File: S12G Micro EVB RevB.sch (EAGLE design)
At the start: 42 parts, among them IC1 FT232RL, IC2 MCP1640, J1 JUMPER_2WAY, J2 JUMPER, J3 JUMPER

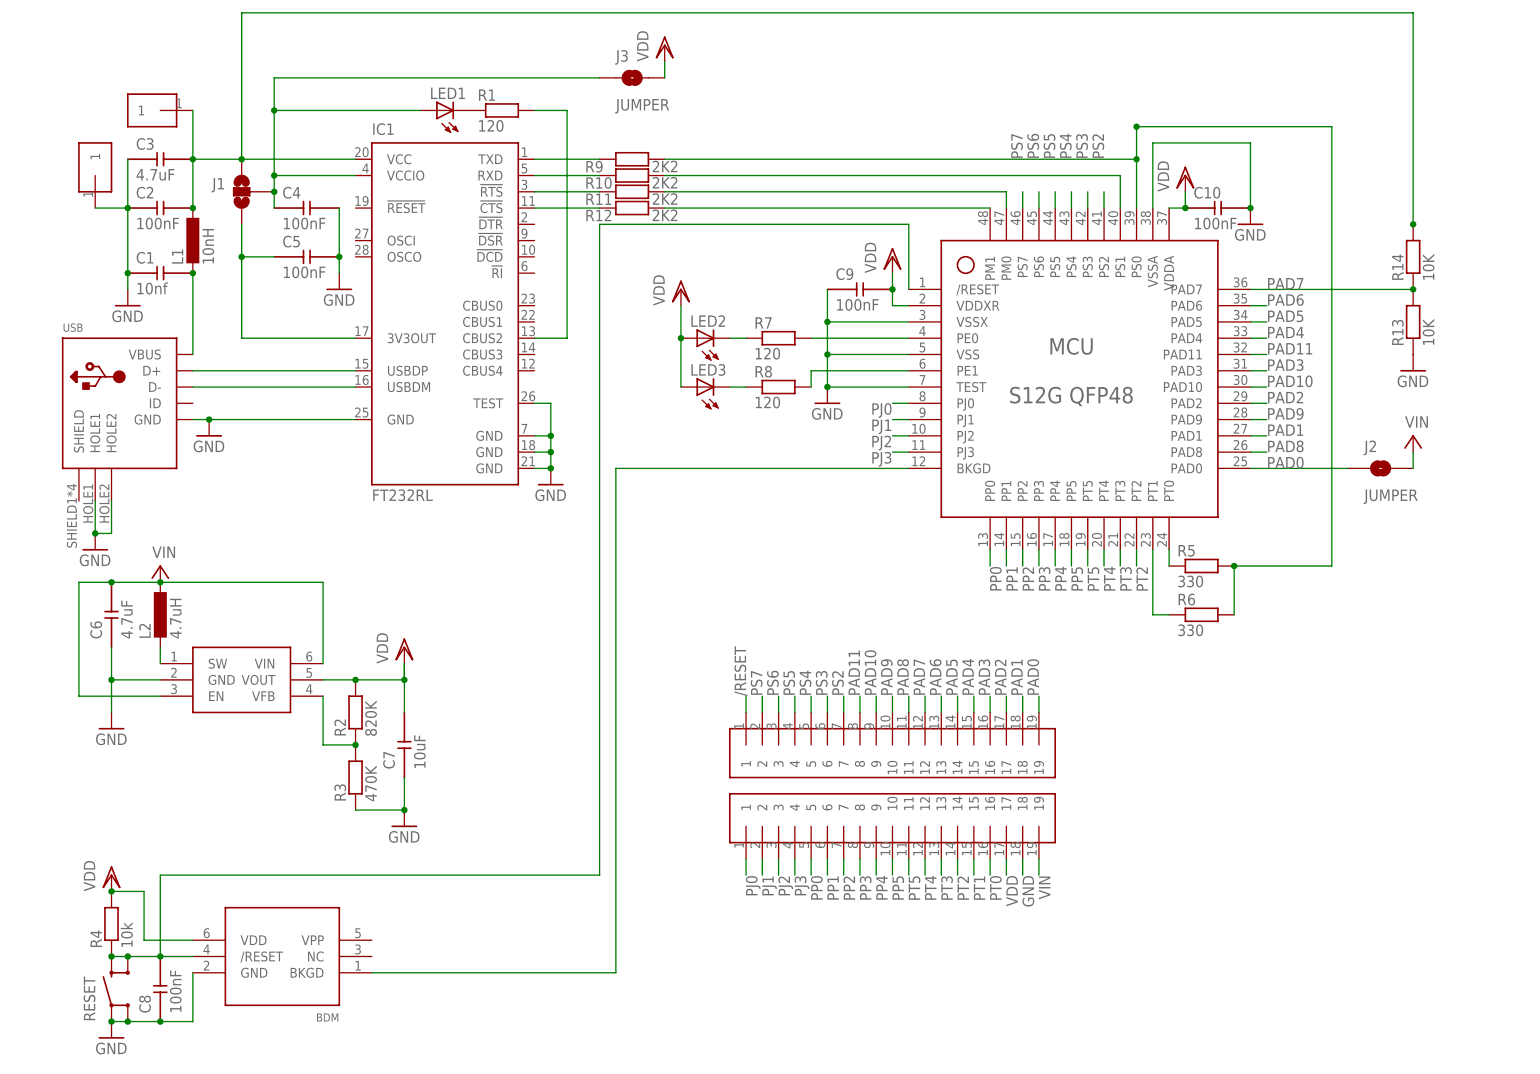
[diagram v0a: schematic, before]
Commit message: finished RevB layout
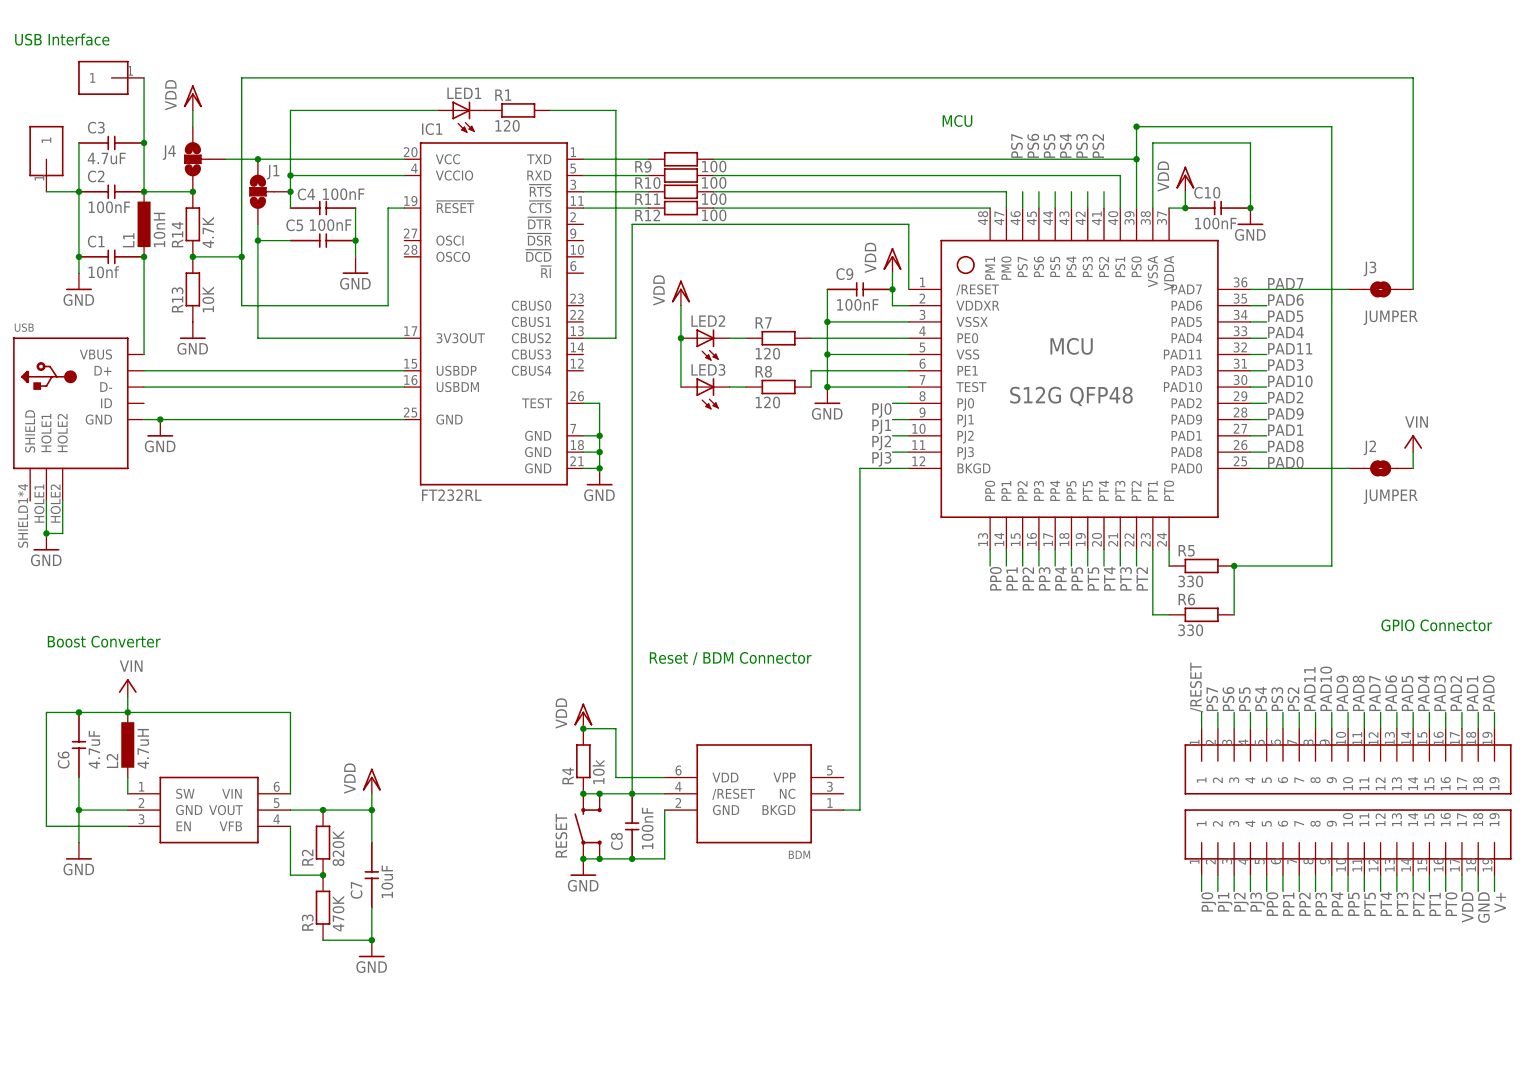
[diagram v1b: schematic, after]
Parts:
- added J4: JUMPER_2WAY, myLibrary:JUMPER_2WAY
- R10, R11, R12, R9: value 2K2 -> 100
- R14: value 10K -> 4.7K
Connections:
- net VIN renamed V+
- new net N$4: IC1.!RESET, J3.2, R13.1, R14.2
- new net VCC: IC1.VCC, J1.1, J4.2
- net PAD7: now also J3.1; no longer R13.1, R14.2
- net VCCIO: no longer J3.1
- net VDD: now also J4.1; no longer J3.2
- net VDDUSB: now also J4.3; no longer IC1.VCC, J1.1
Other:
- note added: "Boost Converter"
- note added: "GPIO Connector"
- note added: "MCU"
- note added: "Reset / BDM Connector"
- note added: "USB Interface"
- moved on the sheet: BDM, C1, C2, C3, C4, C5, C6, C7, C8, IC1, J1, J3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
